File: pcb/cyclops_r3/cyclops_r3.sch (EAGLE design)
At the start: 112 parts, among them Q1 SUM11006, Q2 IRF540, U1 MCP4921, U10 AD829, U11 MIC5225, U12 MIC5270, U2 317-N, U3 TLV37, U4 337-N, U5 ADR03, U6 OP1177, U7 TLV2374, U8 ZXTD45, U9 ADA4899

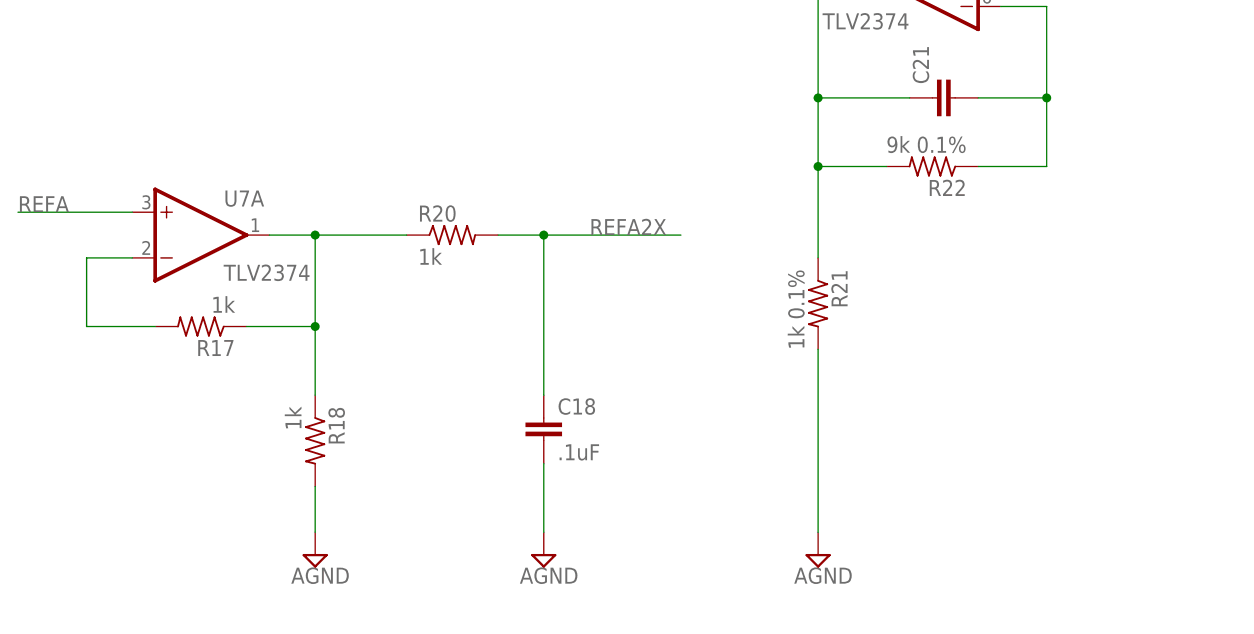
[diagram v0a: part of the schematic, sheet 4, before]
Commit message: Fixed some wiring problems, added some notes.
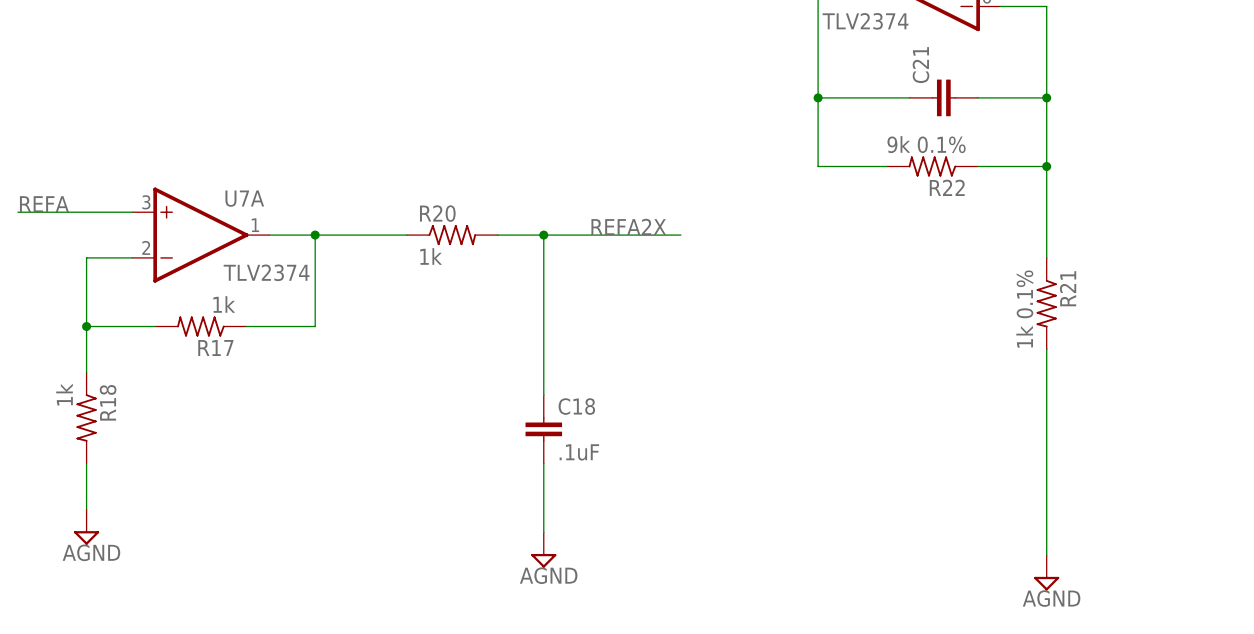
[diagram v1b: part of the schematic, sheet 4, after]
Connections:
- net N$15: now also R21.1
- net N$8: now also R18.1
- net VI: no longer R21.1
- net VREFA2X: no longer R18.1
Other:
- moved on the sheet: R18, R21
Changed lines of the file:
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@@
 <attributes>
 <attribute name="DESIGNER" value="JONATHAN P. NEWMAN"/>
-<attribute name="DOC_NUMBER" value="1.1"/>
+<attribute name="DOC_NUMBER" value="N/A"/>
 <attribute name="REVISION" value="3.1"/>
 </attributes>
@@
 <instance part="CTL_K" gate="1" x="-55.88" y="86.36" rot="MR180"/>
 <instance part="R22" gate="R" x="27.94" y="2.54" rot="R180"/>
-<instance part="R21" gate="R" x="15.24" y="-12.7" rot="R270"/>
+<instance part="R21" gate="R" x="40.64" y="-12.7" rot="R270"/>
 <instance part="RSENSE" gate="R" x="167.64" y="-10.16" rot="R90"/>
-<instance part="SUPPLY22" gate="G$1" x="15.24" y="-40.64"/>
+<instance part="SUPPLY22" gate="G$1" x="40.64" y="-43.18"/>
 <instance part="SUPPLY23" gate="G$1" x="-55.88" y="60.96"/>
 <instance part="SUPPLY24" gate="G$1" x="167.64" y="-40.64"/>
@@
 <instance part="SUPPLY1" gate="G$1" x="134.62" y="45.72"/>
 <instance part="U7" gate="A" x="-53.34" y="-5.08"/>
-<instance part="R18" gate="R" x="-40.64" y="-27.94" rot="R270"/>
+<instance part="R18" gate="R" x="-66.04" y="-25.4" rot="R270"/>
 <instance part="R17" gate="R" x="-53.34" y="-15.24" rot="R180"/>
-<instance part="SUPPLY37" gate="G$1" x="-40.64" y="-40.64"/>
+<instance part="SUPPLY37" gate="G$1" x="-66.04" y="-38.1"/>
 <instance part="R20" gate="R" x="-25.4" y="-5.08"/>
 <instance part="C18" gate="C" x="-15.24" y="-25.4"/>
@@
 <wire x1="15.24" y1="10.16" x2="15.24" y2="2.54" width="0.1524" layer="91"/>
 <wire x1="15.24" y1="2.54" x2="22.86" y2="2.54" width="0.1524" layer="91"/>
-<pinref part="R21" gate="R" pin="1"/>
-<wire x1="15.24" y1="-7.62" x2="15.24" y2="2.54" width="0.1524" layer="91"/>
-<junction x="15.24" y="2.54"/>
 <label x="-73.66" y="22.86" size="1.778" layer="95"/>
 <pinref part="S5" gate="G$1" pin="1"/>
@@
 <wire x1="33.02" y1="10.16" x2="40.64" y2="10.16" width="0.1524" layer="91"/>
 <junction x="40.64" y="10.16"/>
+<pinref part="R21" gate="R" pin="1"/>
+<wire x1="40.64" y1="-7.62" x2="40.64" y2="2.54" width="0.1524" layer="91"/>
+<junction x="40.64" y="2.54"/>
 </segment>
 </net>
@@
 <segment>
 <pinref part="R21" gate="R" pin="2"/>
-<wire x1="15.24" y1="-17.78" x2="15.24" y2="-38.1" width="0.1524" layer="91"/>
+<wire x1="40.64" y1="-17.78" x2="40.64" y2="-40.64" width="0.1524" layer="91"/>
 <pinref part="SUPPLY22" gate="G$1" pin="AGND"/>
 </segment>
@@
 <pinref part="SUPPLY37" gate="G$1" pin="AGND"/>
 <pinref part="R18" gate="R" pin="2"/>
-<wire x1="-40.64" y1="-38.1" x2="-40.64" y2="-33.02" width="0.1524" layer="91"/>
+<wire x1="-66.04" y1="-35.56" x2="-66.04" y2="-30.48" width="0.1524" layer="91"/>
 </segment>
 <segment>
@@
 <pinref part="R17" gate="R" pin="1"/>
 <wire x1="-48.26" y1="-15.24" x2="-40.64" y2="-15.24" width="0.1524" layer="91"/>
-<pinref part="R18" gate="R" pin="1"/>
-<wire x1="-40.64" y1="-15.24" x2="-40.64" y2="-22.86" width="0.1524" layer="91"/>
-<junction x="-40.64" y="-15.24"/>
 <pinref part="R20" gate="R" pin="1"/>
 </segment>
@@
 <pinref part="R17" gate="R" pin="2"/>
 <wire x1="-66.04" y1="-15.24" x2="-58.42" y2="-15.24" width="0.1524" layer="91"/>
-</segment>
-</net>
+<pinref part="R18" gate="R" pin="1"/>
+<wire x1="-66.04" y1="-20.32" x2="-66.04" y2="-15.24" width="0.1524" layer="91"/>
+<junction x="-66.04" y="-15.24"/>
+</segment>
+</net>

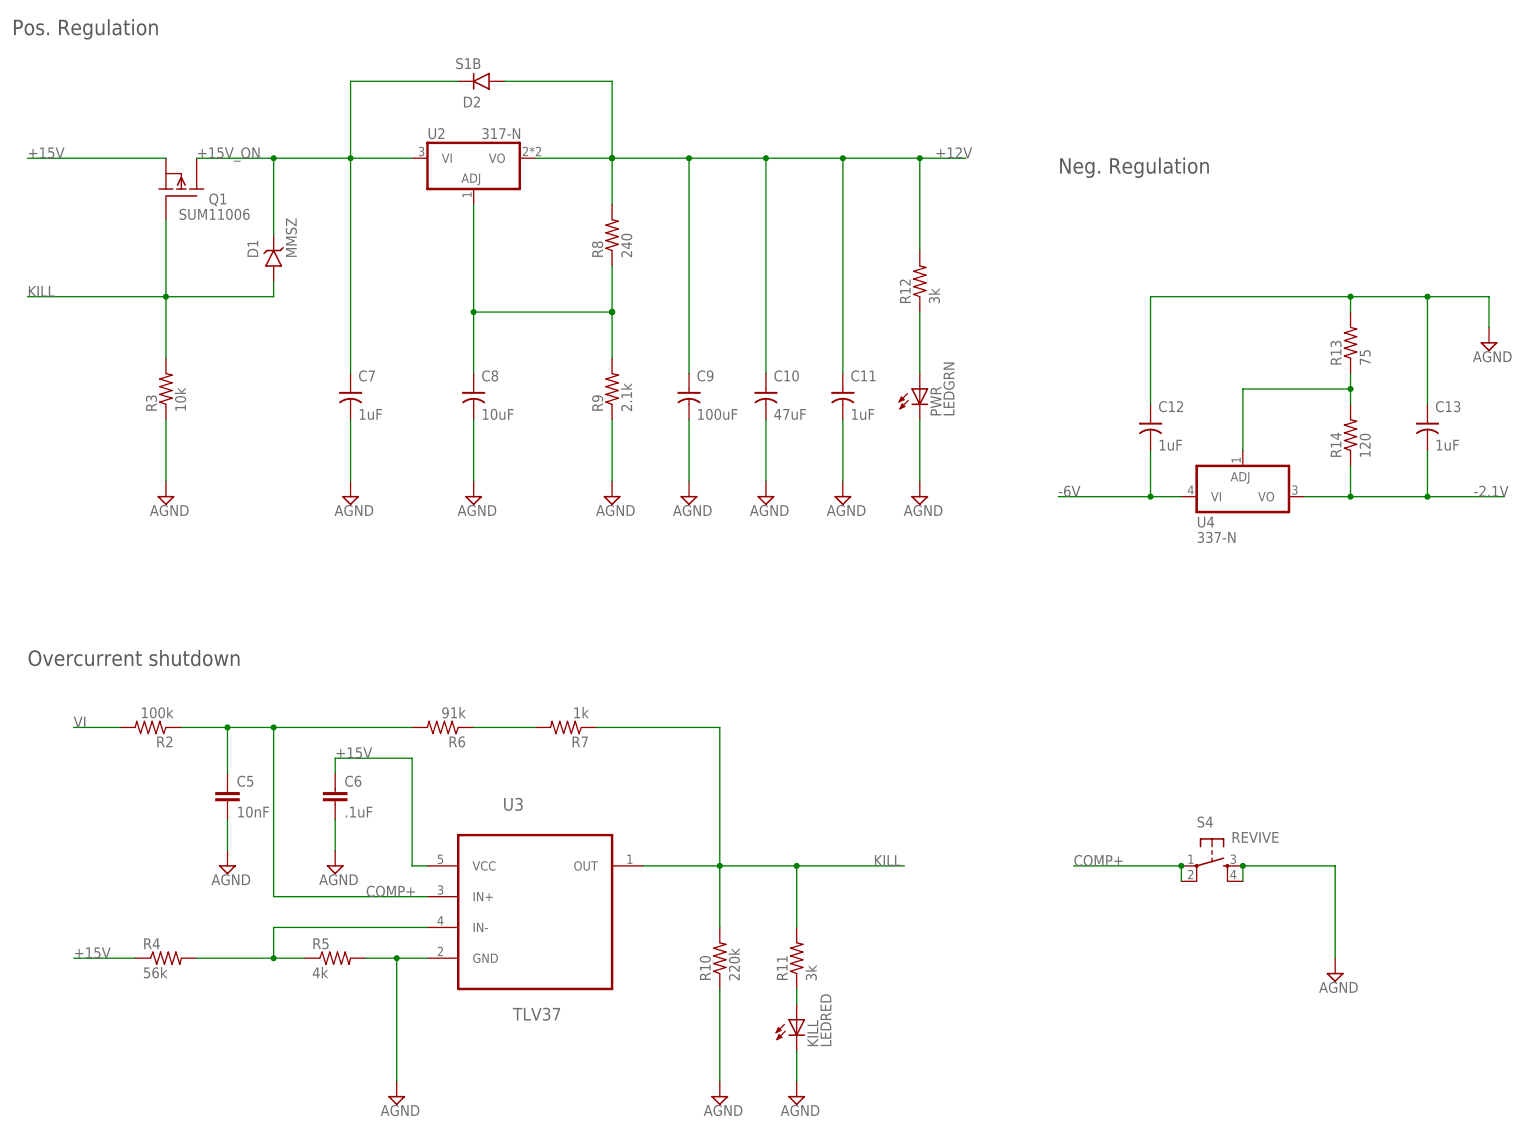
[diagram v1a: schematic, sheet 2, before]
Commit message: More revisions due to circuit assembly and UI considerations. More design notes.
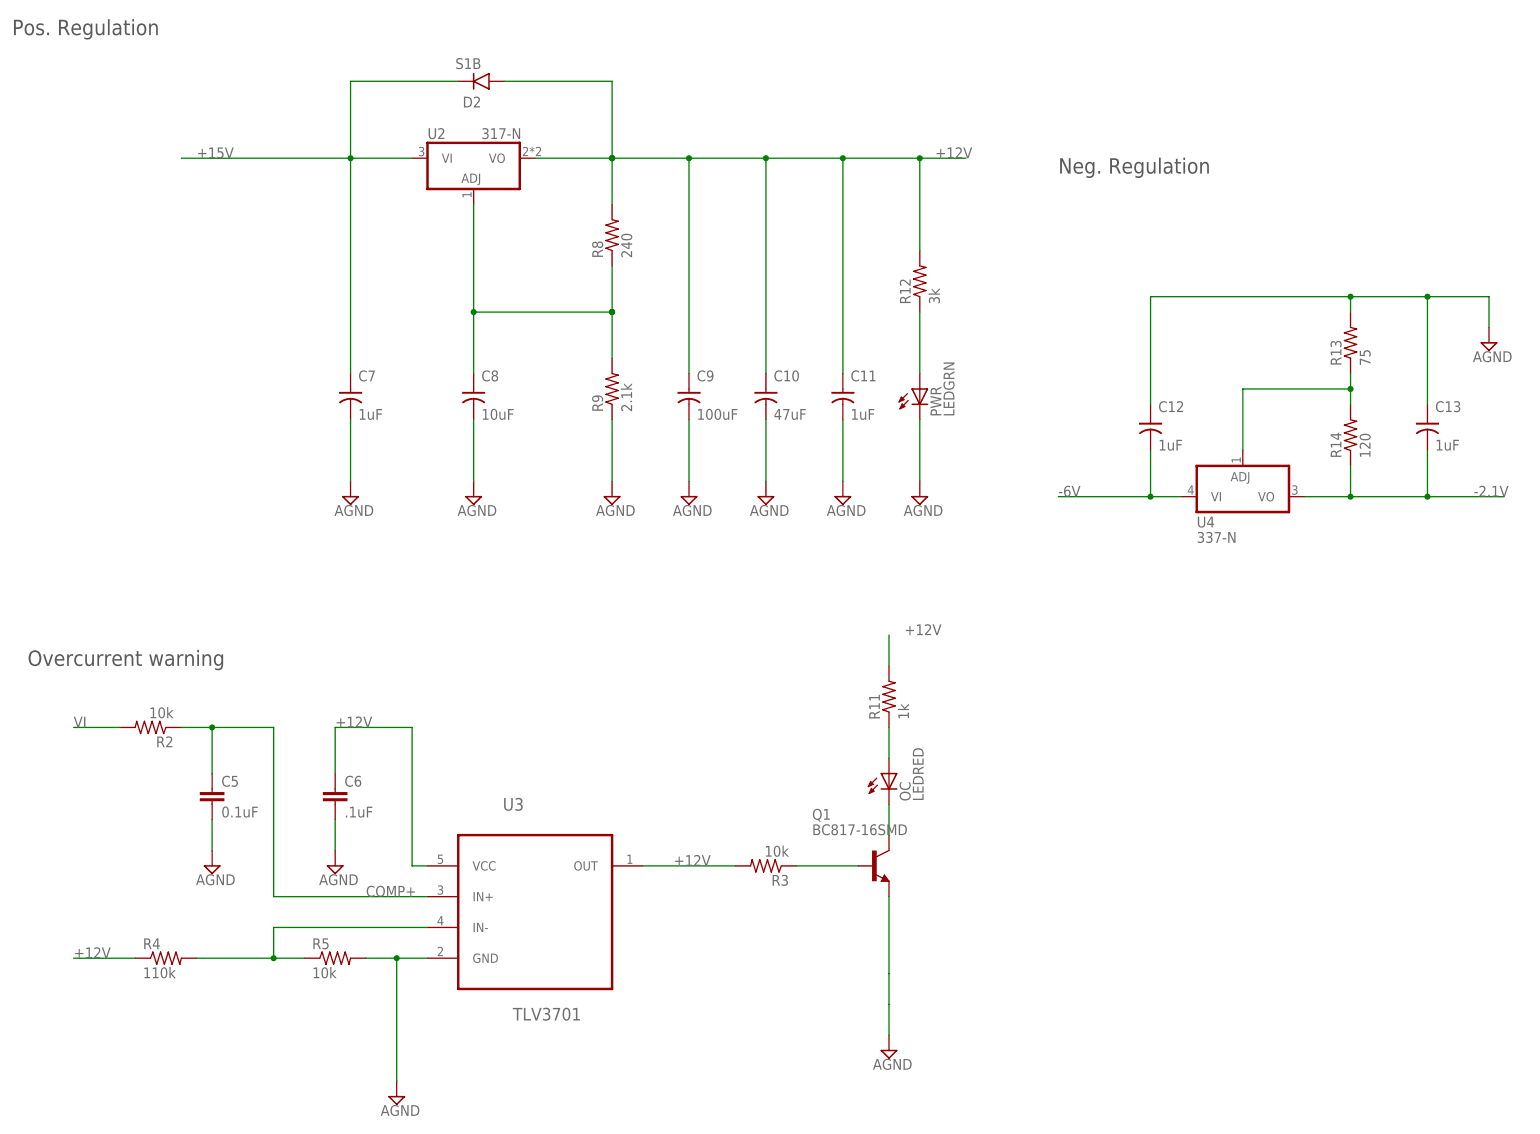
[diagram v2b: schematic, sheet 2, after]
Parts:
- removed BIAS: 10k, cyclops:TRIM_US-SM-42/43W
- removed D1: MMSZ, cyclops:Z-DIODE_MMSZ
- removed KILL: LEDRED, cyclops:LEDRED_0805
- removed R10: 220k, cyclops:R_0603
- removed R6: 91k, cyclops:R_0603
- removed R7: 1k, cyclops:R_0603
- removed S2: 219-04, cyclops:219-04
- removed S4: REVIVE, jonnew-eagle:SPST_TACT-B3F
- added C36: .1uF, cyclops:C_0603
- added CS0, CS1, CS2, CS3, TMP0, TMP1, TMP2, TMP3: (no value), cyclops:SJ
- added OC: LEDRED, cyclops:LEDRED_0805
- C22: value .1uF -> 1uF; device cyclops:C_0603 -> cyclops:C_0805
- C5: value 10nF -> 0.1uF
- Q1: value SUM11006 -> BC817-16SMD; device cyclops:SUM110P06_TO-262 -> cyclops:BC817-16SMD
- R11: value 3k -> 1k
- R2: value 100k -> 10k
- R4: value 56k -> 110k
- R5: value 4k -> 10k
- U3: value TLV37 -> TLV3701
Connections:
- removed net +15V_ON: C7.+, D1.C, D2.C, Q1.D, U2.VI
- removed net KILL: D1.A, Q1.G, R10.2, R11.2, R3.2, R7.1, U3.OUT
- removed net N$11: KILL.A, R11.1
- new net CS4: ARDUNIO.A0, TMP0.1
- new net CS5: ARDUNIO.A1, TMP1.1
- new net CS6: ARDUNIO.A3, TMP3.1
- new net CS8: ARDUNIO.A2, TMP2.1
- new net LED+: Q2.S
- new net N$27: R3.2, U3.OUT
- new net N$28: Q1.B, R3.1
- net +12V: now also C6.1, Q2.D, R11.2, R4.1, U3.VCC; no longer BIAS.A, C22.1
- net +15V: now also C7.+, D2.C, U2.VI; no longer C6.1, Q1.S, R4.1, U3.VCC
- net -2.1V: now also C22.1, C36.1; no longer C19.2, C20.2
- net AGND: now also C19.2, C20.2, C22.2, C36.2, Q1.E
- net COMP+: no longer R6.2, S4.P, S4.P1
- net CS: now also CS0.2, CS1.2, CS2.2, CS3.2; no longer S2.1, S2.2, S2.3, S2.4
- net CS0: now also ARDUNIO.D2, CS0.1; no longer ARDUNIO.D0, S2.5
- net CS1: now also ARDUNIO.D3, CS1.1; no longer ARDUNIO.D1, S2.6
- net CS2: now also ARDUNIO.D4, CS2.1; no longer ARDUNIO.D2, S2.7
- net CS3: now also ARDUNIO.D5, CS3.1; no longer ARDUNIO.D3, S2.8
- net GND: no longer BIAS.E, C22.2, KILL.C, R10.1, R3.1, S4.S, S4.S1
- net LDAC: now also ARDUNIO.D6; no longer ARDUNIO.D4
- net LED-: now also RSENSE.2, U7B.+IN; no longer Q2.D
- net N$2: now also OC.A, R11.1; no longer Q2.S, RSENSE.2, U7B.+IN
- net N$4: no longer BIAS.S
- net N$9: now also OC.C, Q1.C; no longer R6.1, R7.2
- net TEMP: now also TMP0.2, TMP1.2, TMP2.2, TMP3.2
- net VTEMP: no longer I/O_BLOCK.6
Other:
- note added: "Overcurrent warning"
- note removed: "Overcurrent shutdown"
- moved on the sheet: C19, C20, C22, C5, Q1, Q2, R11, R3, RSENSE

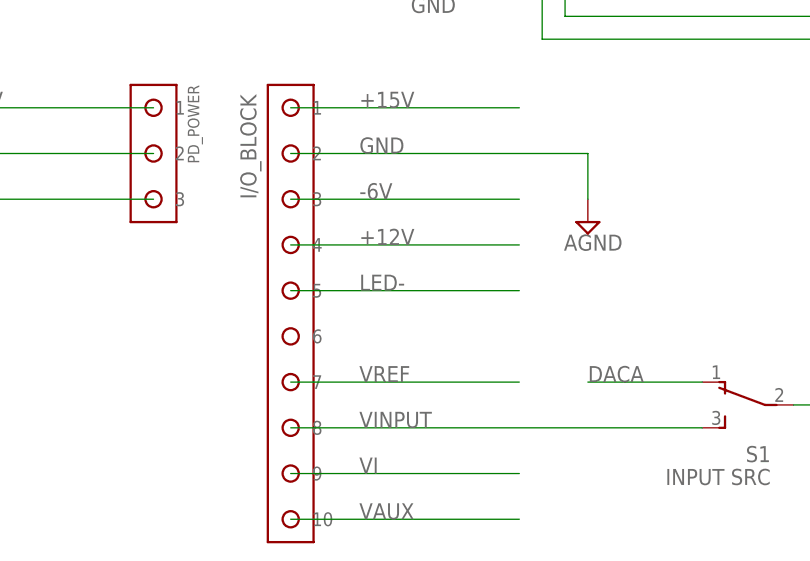
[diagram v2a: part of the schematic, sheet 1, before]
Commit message: Making fixes based on previous assembly.
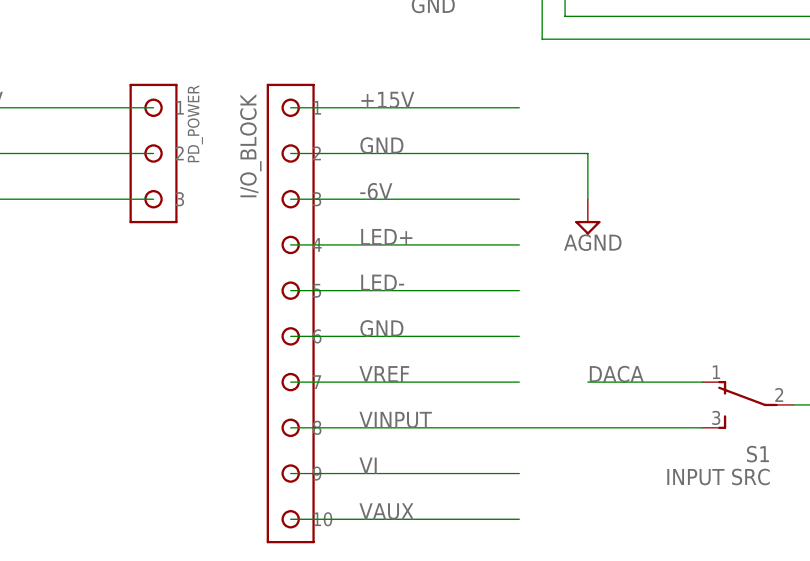
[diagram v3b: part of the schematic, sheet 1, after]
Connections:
- net +12V: no longer I/O_BLOCK.4
- net GND: now also I/O_BLOCK.6
- net LED+: now also I/O_BLOCK.4
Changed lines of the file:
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@@
 <?xml version="1.0" encoding="utf-8"?>
 <!DOCTYPE eagle SYSTEM "eagle.dtd">
-<eagle version="6.5.0">
+<eagle version="6.4">
 <drawing>
 <settings>
@@
 <label x="5.08" y="-10.16" size="1.778" layer="95"/>
 </segment>
+<segment>
+<pinref part="I/O_BLOCK" gate="G$1" pin="6"/>
+<wire x1="43.18" y1="-30.48" x2="68.58" y2="-30.48" width="0.1524" layer="91"/>
+<label x="50.8" y="-30.48" size="1.778" layer="95"/>
+</segment>
 </net>
 <net name="VAUX" class="0">
@@
 </net>
 <net name="+12V" class="1">
-<segment>
-<pinref part="I/O_BLOCK" gate="G$1" pin="4"/>
-<wire x1="43.18" y1="-20.32" x2="68.58" y2="-20.32" width="0.1524" layer="91"/>
-<label x="50.8" y="-20.32" size="1.778" layer="95"/>
-</segment>
 <segment>
 <pinref part="PD_POWER" gate="G$1" pin="1"/>
@@
 </segment>
 </net>
+<net name="LED+" class="0">
+<segment>
+<pinref part="I/O_BLOCK" gate="G$1" pin="4"/>
+<wire x1="43.18" y1="-20.32" x2="68.58" y2="-20.32" width="0.1524" layer="91"/>
+<label x="50.8" y="-20.32" size="1.778" layer="95"/>
+</segment>
+</net>
